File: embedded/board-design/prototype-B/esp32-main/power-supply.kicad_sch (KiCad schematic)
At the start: 25 parts, among them J6 Conn_01x03_Socket, J7 Conn_01x02_Socket, Q3 FDN340P, Q4 FMMT720TA, U4 TPS61090

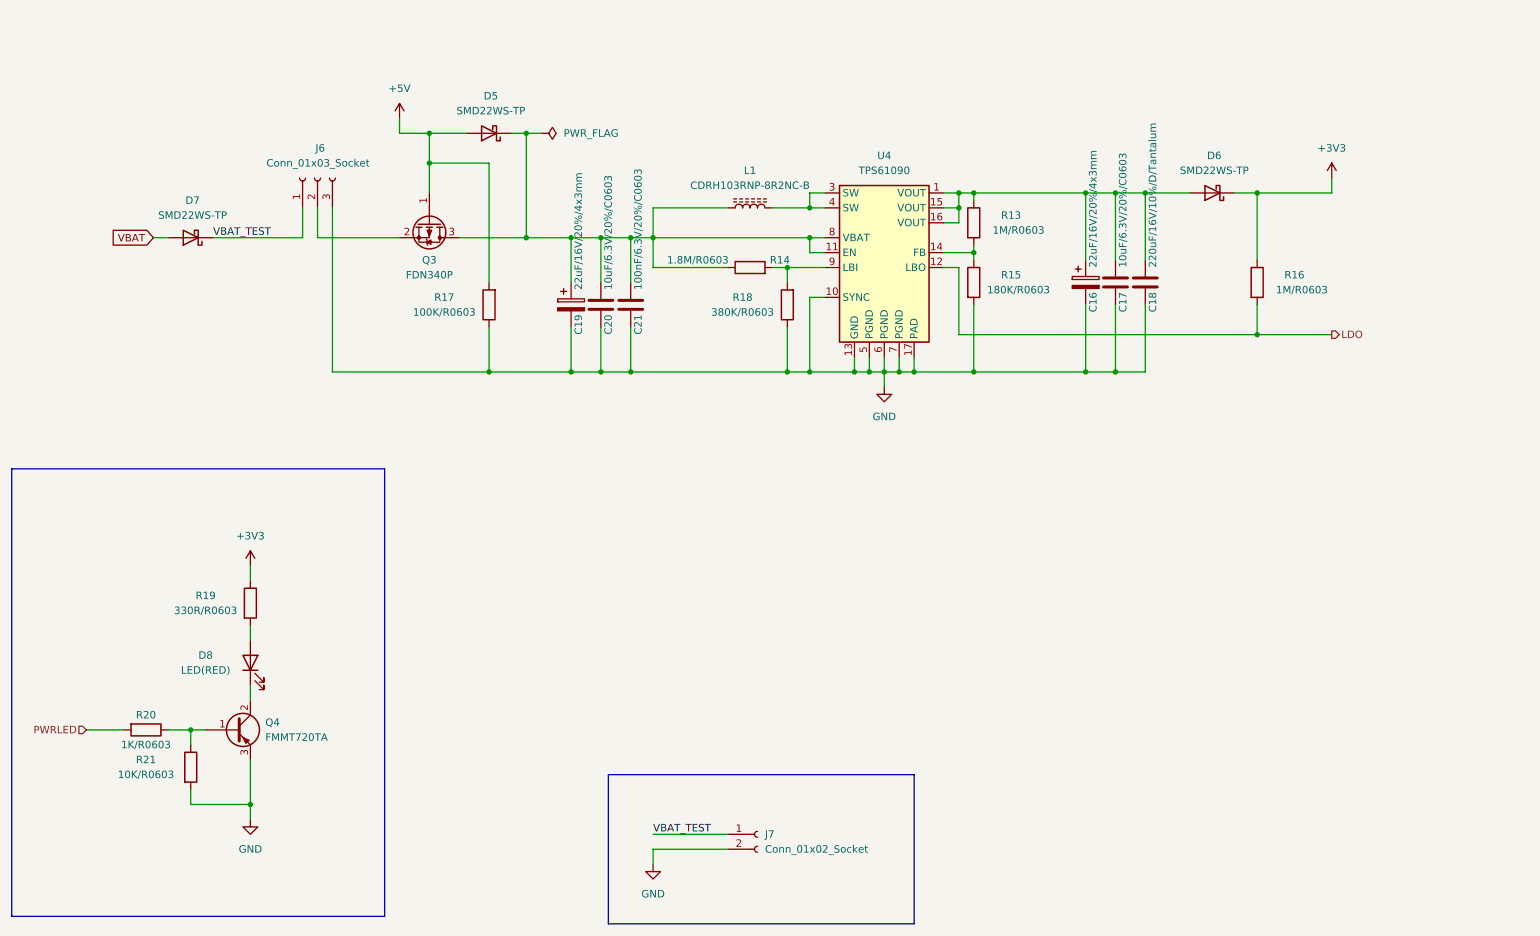
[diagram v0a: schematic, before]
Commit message: [prototype-B]
Refactored power scheme.

Signed-off-by: Nicolae-Andrei Vasile <vasilenicolaeandrei@gmail.com>
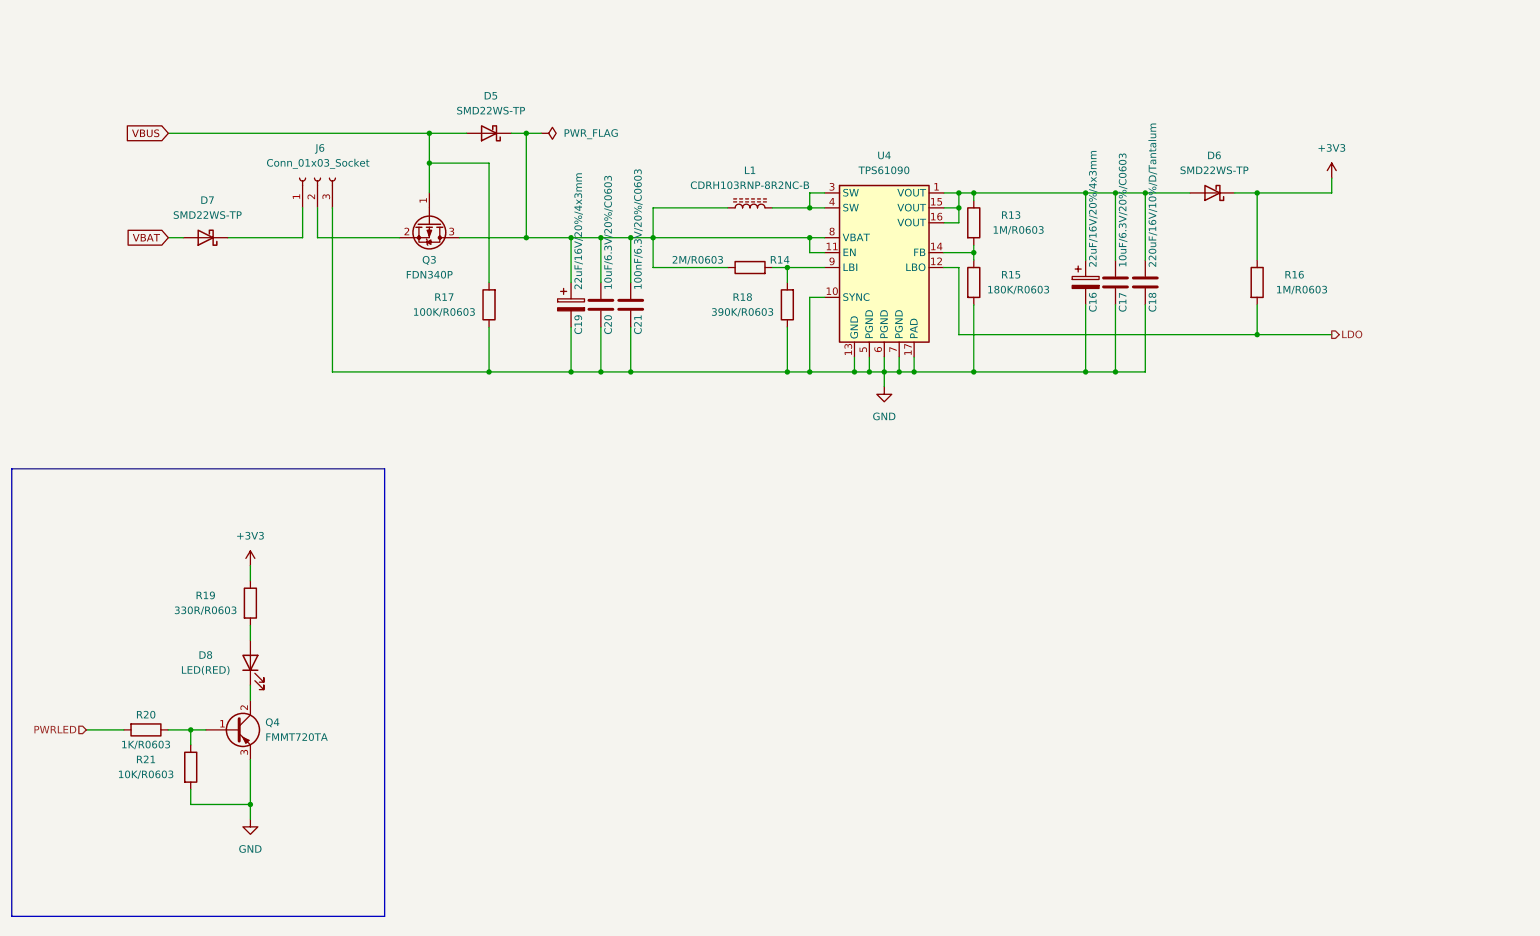
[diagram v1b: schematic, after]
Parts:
- removed J7: Conn_01x02_Socket, Connector_PinHeader_1.27mm:PinHeader_1x02_P1.27mm_Vertical, symbol Connector:Conn_01x02_Socket
- R14: value 1.8M/R0603 -> 2M/R0603
- R18: value 380K/R0603 -> 390K/R0603
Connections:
- net +5V renamed VBUS
- net VBAT_TEST: no longer names the net of D7.1 (K), J6.1 (Pin_1)
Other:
- moved on the sheet: D7

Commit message: [prototype-B]
Refactored power scheme. Updated prototype-B README.md.

Signed-off-by: Nicolae-Andrei Vasile <vasilenicolaeandrei@gmail.com>
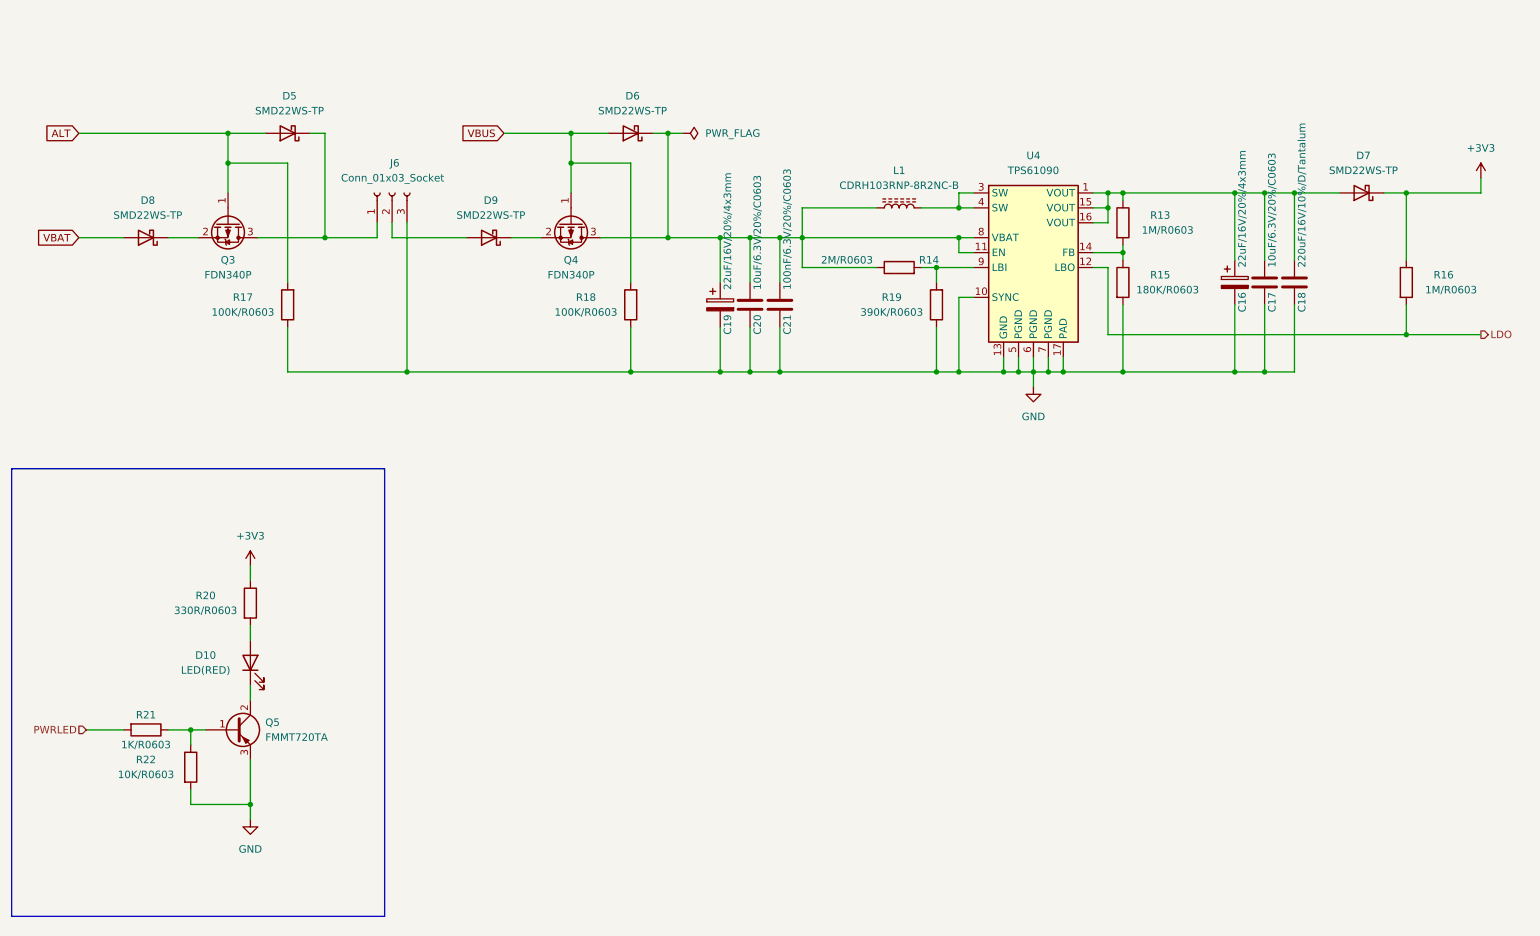
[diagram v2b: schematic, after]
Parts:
- added D6, D9: SMD22WS-TP, Diode_SMD:D_SOD-323_HandSoldering, symbol Device:D_Schottky
- added Q4: FDN340P, Package_TO_SOT_SMD:SOT-23, symbol Transistor_FET:FDN340P
- added R18: 100K/R0603, Resistor_SMD:R_0603_1608Metric_Pad0.98x0.95mm_HandSolder, symbol Device:R
- renumbered D8 to D10, D6 to D7, D7 to D8, Q4 to Q5, R18 to R19, R19 to R20, R20 to R21, R21 to R22
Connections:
- net GND: now also R18.1
- net VBUS: now also D6.2 (A), Q4.1 (G), R18.2; no longer D5.2 (A), Q3.1 (G), R17.2
- net at C19.1, C20.1, C21.1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: now also D6.1 (K), Q4.3 (D); no longer D5.1 (K), Q3.3 (D)
- net at D8.1 (K): now also Q3.2 (S); no longer J6.1 (Pin_1)
- net at J6.2 (Pin_2): now also D9.2 (A); no longer Q3.2 (S)
- new net: D5.1 (K), J6.1 (Pin_1), Q3.3 (D)
- new net: D9.1 (K), Q4.2 (S)
- new net ALT: D5.2 (A), Q3.1 (G), R17.2
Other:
- moved on the sheet: C16, C17, C18, C19, C20, C21, D5, D7, D8, J6, L1, Q3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

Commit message: [prototype-B]
Refactored hardware implementation.

Signed-off-by: Nicolae-Andrei Vasile <vasilenicolaeandrei@gmail.com>
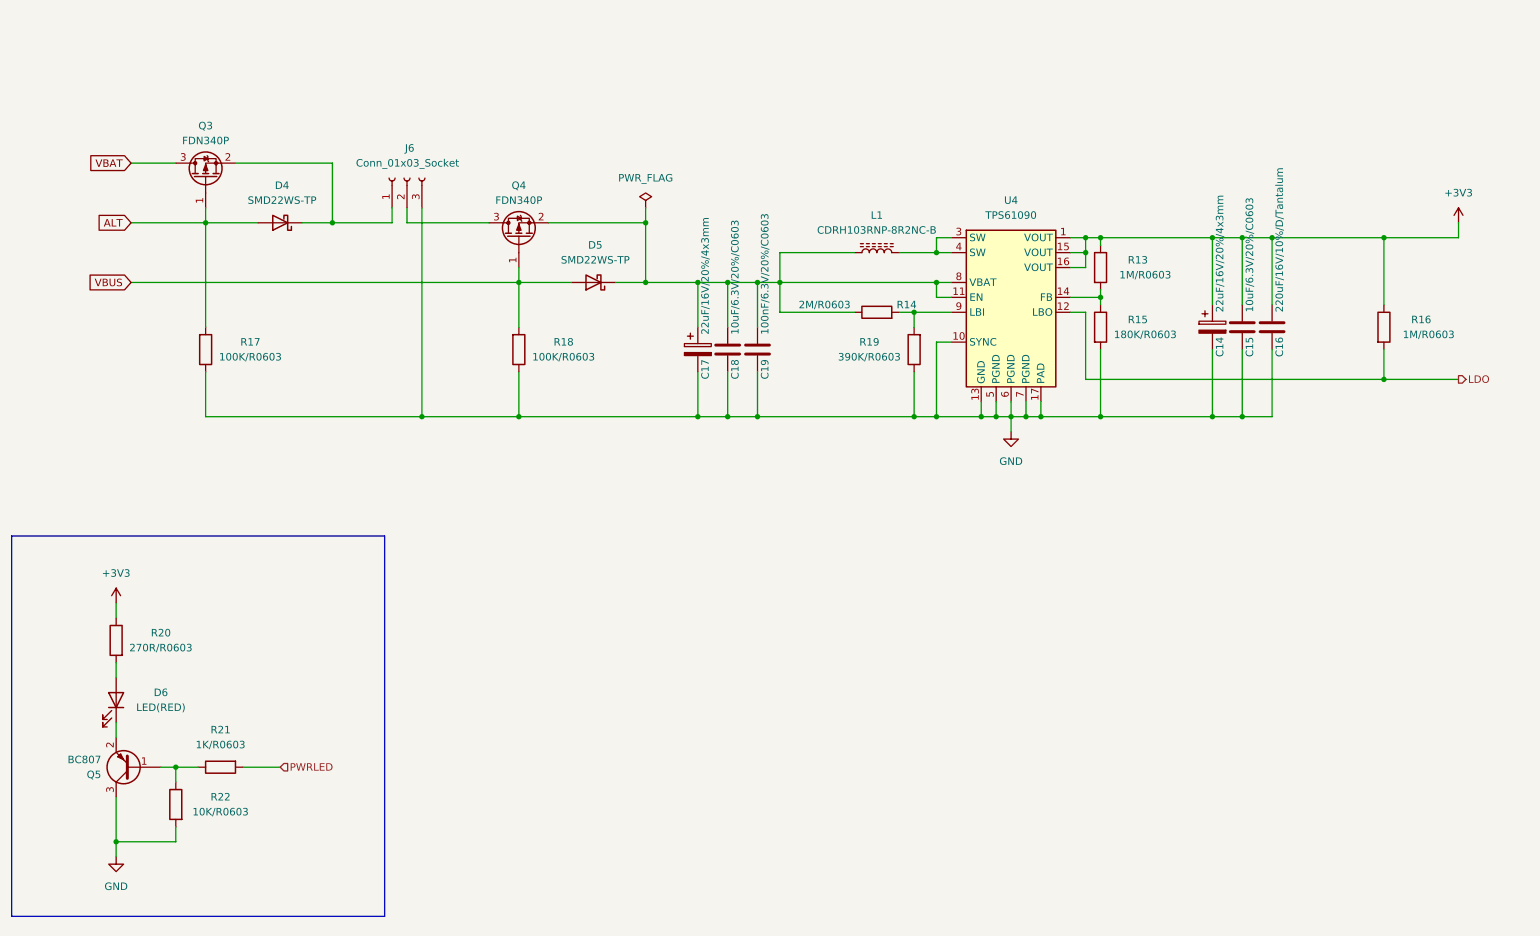
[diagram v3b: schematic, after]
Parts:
- removed D6, D7, D8, D9: SMD22WS-TP, Diode_SMD:D_SOD-323_HandSoldering, symbol Device:D_Schottky
- removed Q5: FMMT720TA, Package_TO_SOT_SMD:TSOT-23, symbol Device:Q_PNP_BCE
- added D4: SMD22WS-TP, Diode_SMD:D_SOD-323_HandSoldering, symbol Device:D_Schottky
- added Q5: BC807, Package_TO_SOT_SMD:SOT-23, symbol Transistor_BJT:BC807
- R20: value 330R/R0603 -> 270R/R0603
- renumbered C16 to C14, C17 to C15, C18 to C16, C19 to C17, C20 to C18, C21 to C19, D10 to D6
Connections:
- net +3V3: now also C14.1, C15.1, C16.1, R13.1, U4.1 (VOUT), U4.15 (VOUT), U4.16 (VOUT)
- net ALT: now also D4.2 (A); no longer D5.2 (A)
- net GND: now also Q5.3 (C)
- net VBAT: now also Q3.3 (D)
- net VBUS: now also D5.2 (A)
- net at C17.1, C18.1, C19.1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: now also D5.1 (K), Q4.2 (S); no longer Q4.3 (D)
- net at R21.1, R22.1: now also Q5.1 (B)
- net at Q3.2 (S): now also J6.1 (Pin_1), D4.1 (K)
- net at J6.2 (Pin_2): now also Q4.3 (D)
- net at D6.1 (K): now also Q5.2 (E)
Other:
- moved on the sheet: C14, C15, C16, C17, C18, C19, D6, J6, L1, R13, R14, R15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

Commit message: [prototype-B]
Refactored hardware implementation. Reduced board size.

Signed-off-by: Nicolae-Andrei Vasile <vasilenicolaeandrei@gmail.com>
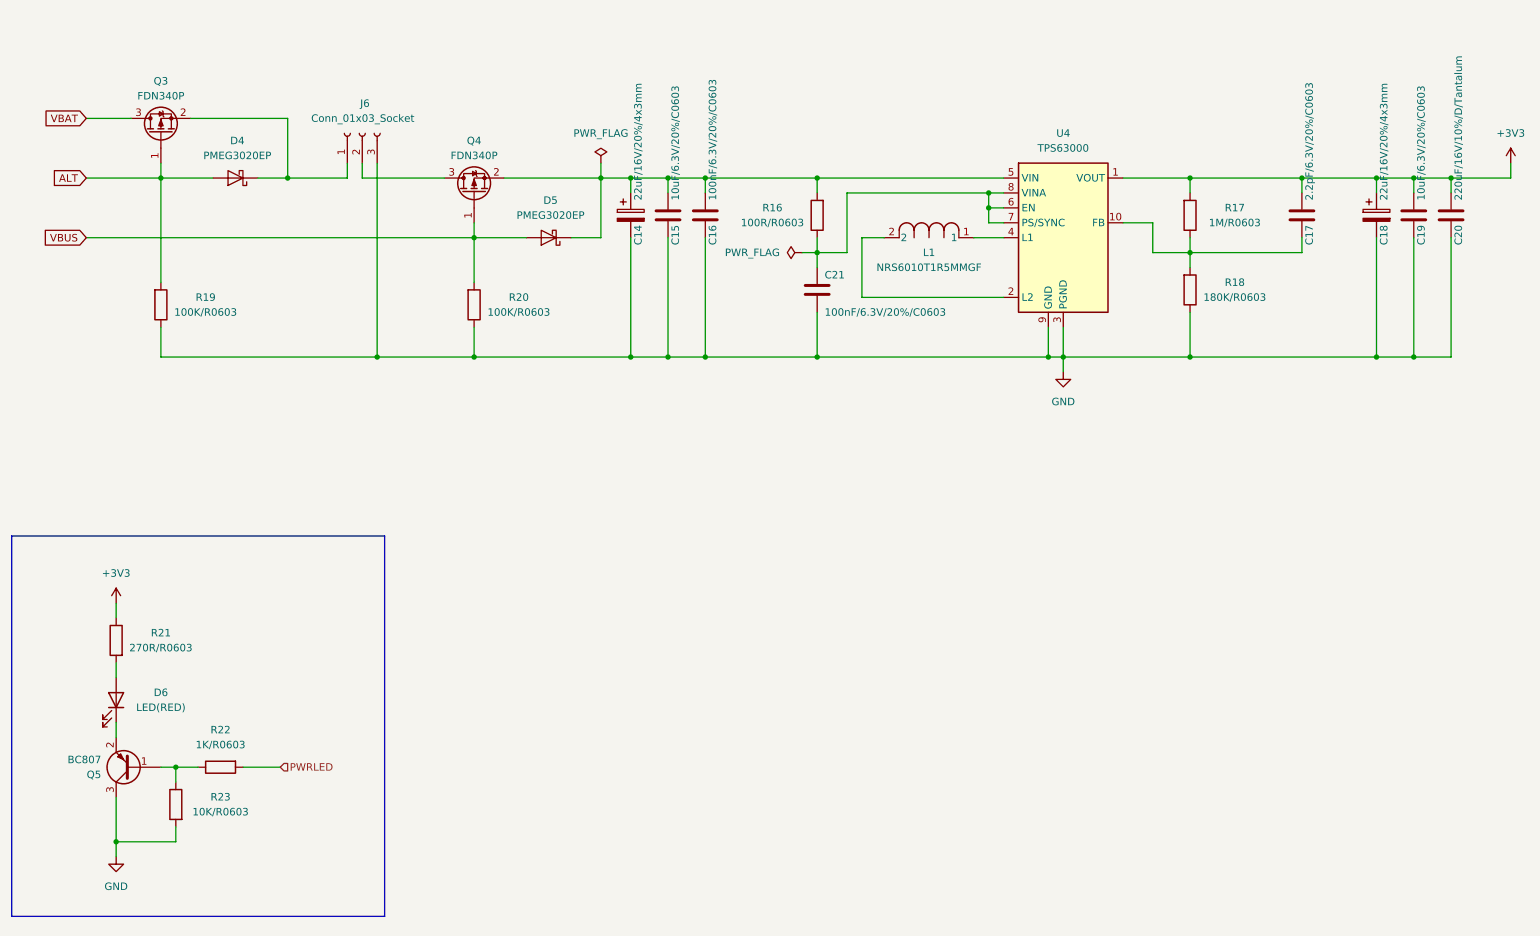
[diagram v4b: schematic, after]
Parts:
- removed D4, D5: SMD22WS-TP, Diode_SMD:D_SOD-323_HandSoldering, symbol Device:D_Schottky
- removed L1: CDRH103RNP-8R2NC-B, Inductor_SMD:L_10.4x10.4_H4.8, symbol Device:L_Ferrite
- removed R13: 1M/R0603, Resistor_SMD:R_0603_1608Metric_Pad0.98x0.95mm_HandSolder, symbol Device:R
- removed R14: 2M/R0603, Resistor_SMD:R_0603_1608Metric_Pad0.98x0.95mm_HandSolder, symbol Device:R
- removed R15: 180K/R0603, Resistor_SMD:R_0603_1608Metric_Pad0.98x0.95mm_HandSolder, symbol Device:R
- removed R19: 390K/R0603, Resistor_SMD:R_0603_1608Metric_Pad0.98x0.95mm_HandSolder, symbol Device:R
- removed U4: TPS61090, Package_DFN_QFN:Texas_RSA_VQFN-16-1EP_4x4mm_P0.65mm_EP2.7x2.7mm_ThermalVias, symbol Regulator_Switching:TPS61090
- added C17: 2.2pF/6.3V/20%/C0603, Capacitor_SMD:C_0603_1608Metric_Pad1.08x0.95mm_HandSolder, symbol Device:C
- added C21: 100nF/6.3V/20%/C0603, Capacitor_SMD:C_0603_1608Metric_Pad1.08x0.95mm_HandSolder, symbol Device:C
- added D4, D5: PMEG3020EP, Diode_SMD:D_SOD-128, symbol Diode:PMEG3020ER
- added L1: NRS6010T1R5MMGF, footprints:IND_TAIYO_NRS6010_TAY, symbol 2024-10-22_19-12-48:NRS6010T1R5MMGF
- added R17: 1M/R0603, Resistor_SMD:R_0603_1608Metric_Pad0.98x0.95mm_HandSolder, symbol Device:R
- added R18: 180K/R0603, Resistor_SMD:R_0603_1608Metric_Pad0.98x0.95mm_HandSolder, symbol Device:R
- added U4: TPS63000, Package_SON:Texas_DRC0010J_ThermalVias, symbol Regulator_Switching:TPS63000
- J6: footprint Connector_Phoenix_MC:PhoenixContact_MC_1,5_3-G-3.81_1x03_P3.81mm_Horizontal -> TerminalBlock_Phoenix:TerminalBlock_Phoenix_MPT-0,5-3-2.54_1x03_P2.54mm_Horizontal
- R16: value 1M/R0603 -> 100R/R0603
- renumbered C17 to C14, C18 to C15, C19 to C16, C14 to C18, C15 to C19, C16 to C20, R17 to R19, R18 to R20, R20 to R21, R21 to R22, R22 to R23
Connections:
- net LDO is gone; now on an unnamed net: R16.2
- net +3V3: now also C17.1, R17.2, U4.1 (VOUT); no longer R16.1
- net ALT: now also D4.2 (A)
- net GND: now also C21.2, R18.1, U4.11 (PGND), U4.3 (PGND), U4.9 (GND)
- net VBUS: now also D5.2 (A)
- net at C14.1, C15.1, C16.1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: now also D5.1 (K), U4.5 (VIN)
- net at J6.1 (Pin_1), Q3.2 (S): now also D4.1 (K)
- new net: C17.2, R17.1, R18.2, U4.10 (FB)
- new net: L1.2, U4.2 (L2)
- new net: L1.1, U4.4 (L1)
- new net: C21.1, R16.1, U4.6 (EN), U4.7 (PS/SYNC), U4.8 (VINA)
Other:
- moved on the sheet: C14, C15, C16, C18, C19, C20, J6, Q3, Q4, R19, R20
